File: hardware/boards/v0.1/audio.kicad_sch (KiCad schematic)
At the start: 30 parts, among them J10 MIDI_IN, J11 MIDI_OUT, J4 SPKR_L, J5 SPKR_R, J8 LINE_OUT, J9 LINE_IN, U24 MIC, U28 TS5A23159RSE, U29 NAU88C22YG

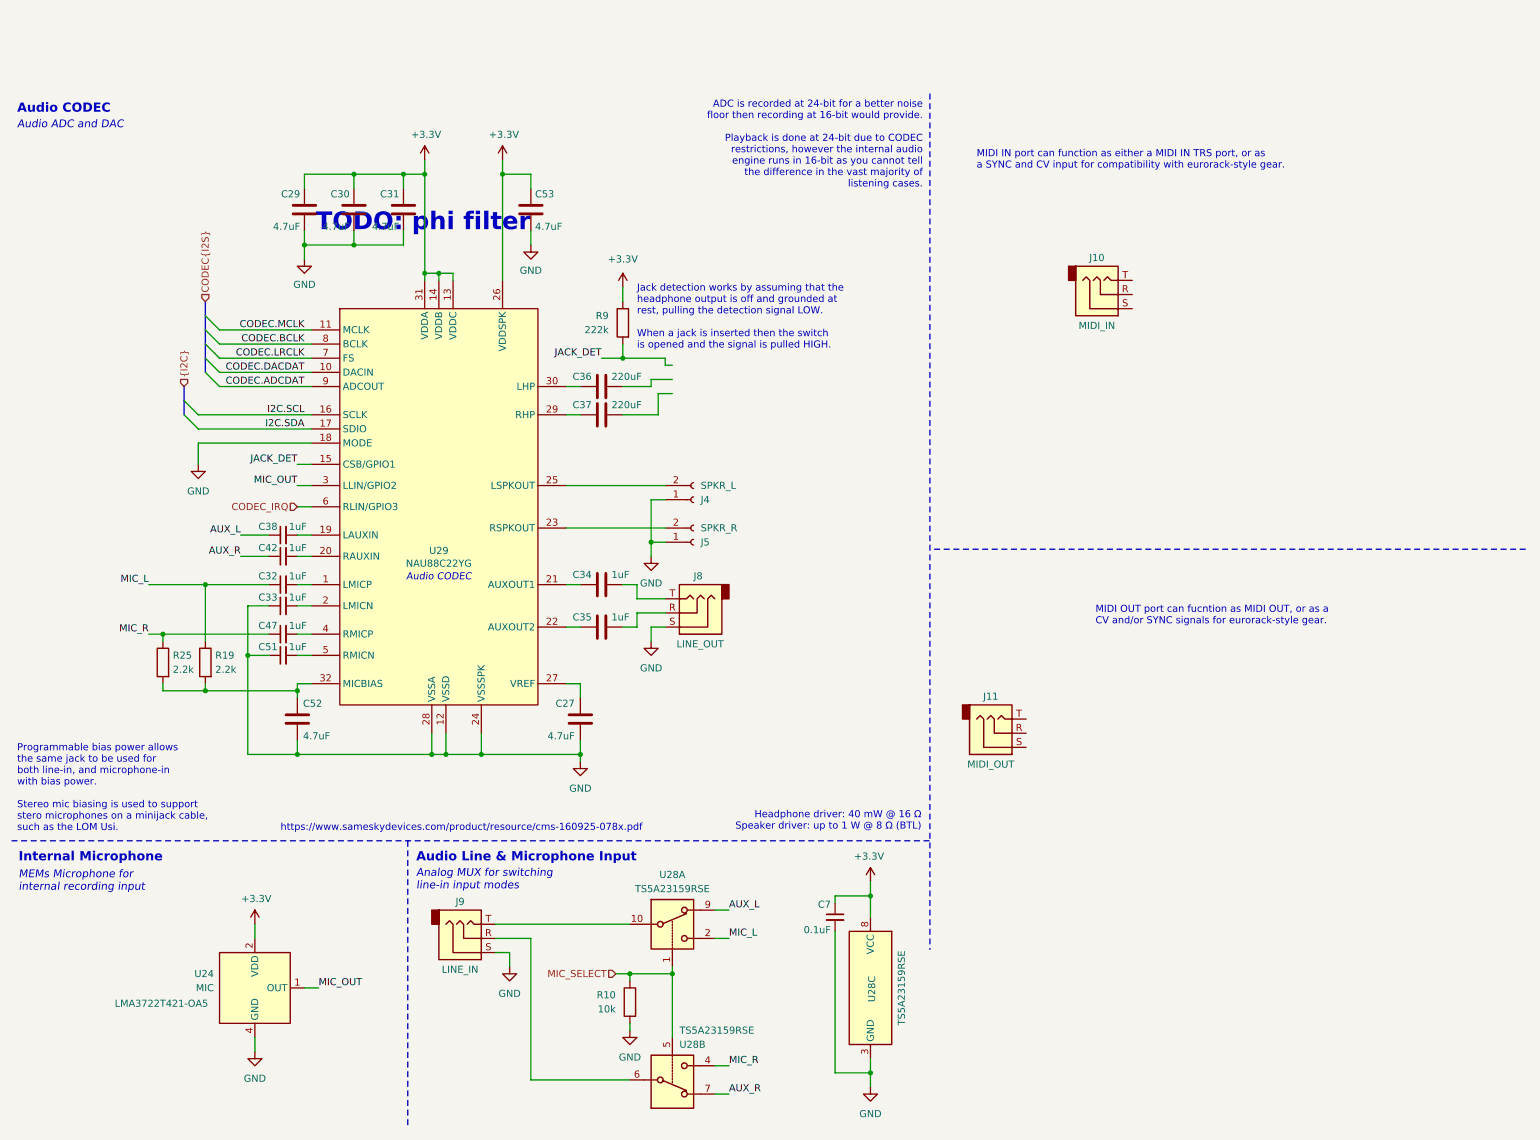
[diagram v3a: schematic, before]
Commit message: feat: start MIDI and CV schematic
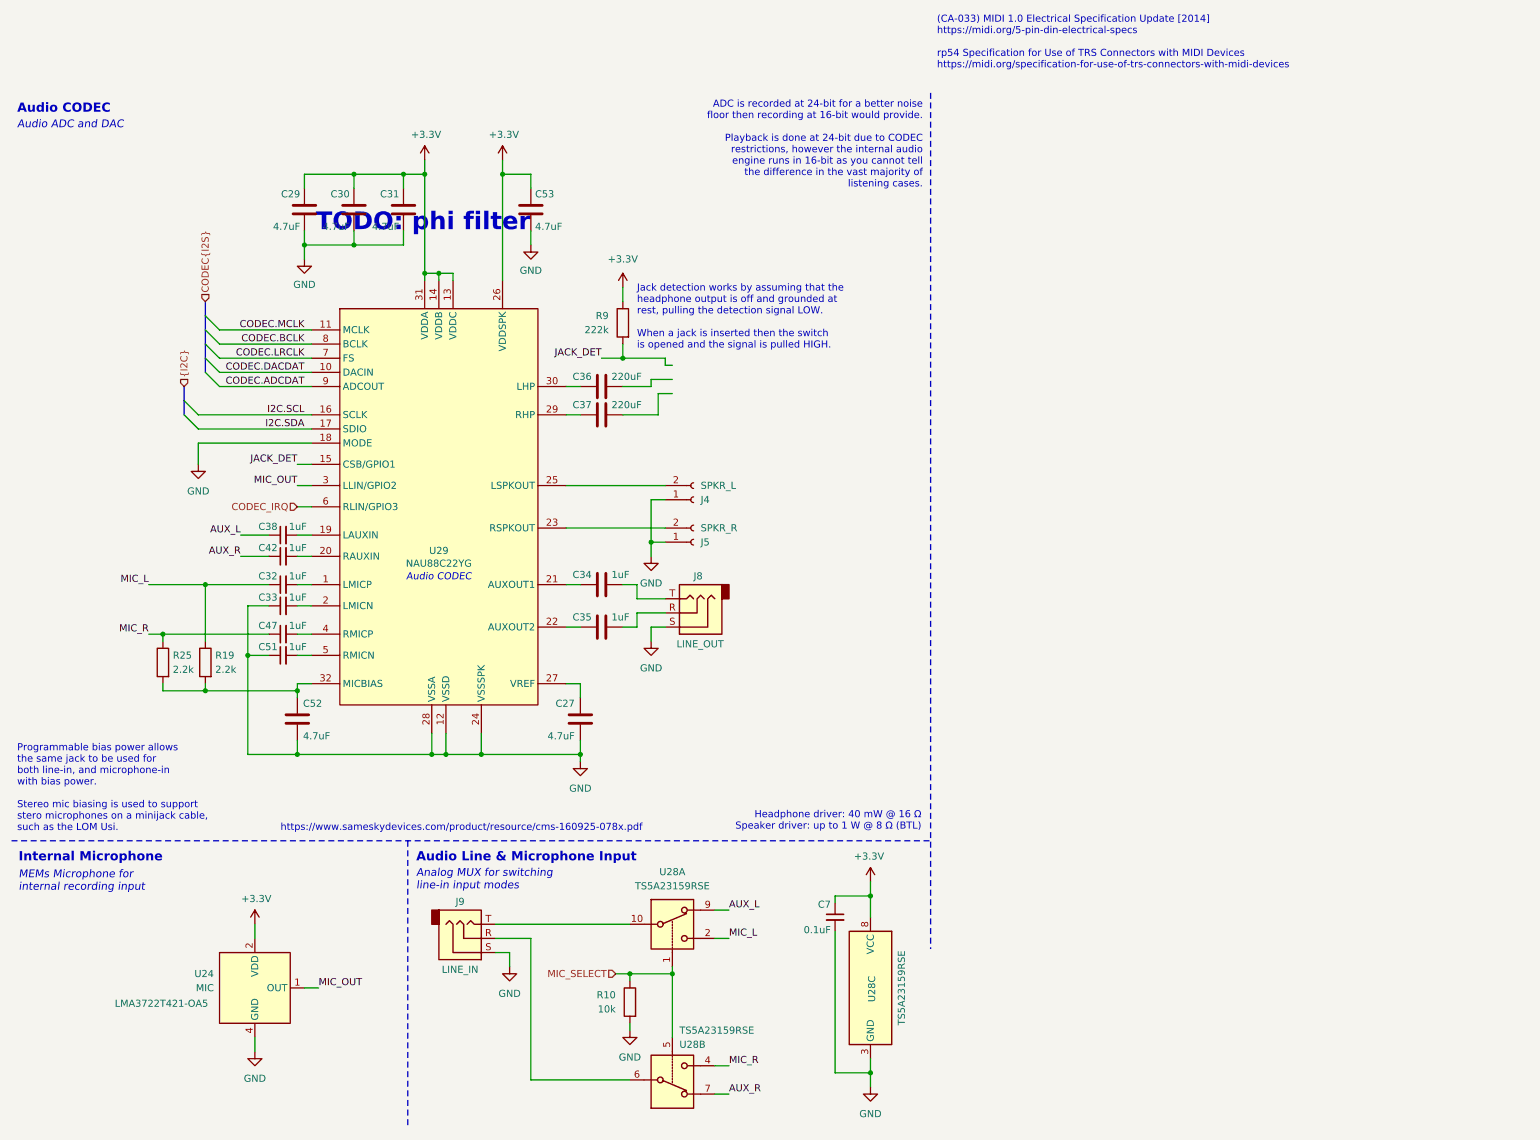
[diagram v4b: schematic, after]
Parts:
- removed J10: MIDI_IN, rhais_connector-lumberg:1503-02, symbol Connector_Audio:AudioJack3
- removed J11: MIDI_OUT, rhais_connector-lumberg:1503-02, symbol Connector_Audio:AudioJack3
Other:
- note added: "(CA-033) MIDI 1.0 Electrical Specification Update [2014] https://midi.org/5-pin-din-electrical-specs rp54 Specification for Use of TRS Connectors with MIDI Devices https://midi.org/specification-for-use-of-trs-connectors-with-midi-devices"
- note removed: "MIDI IN port can function as either a MIDI IN TRS port, or as a SYNC and CV input for compatibility with eurorack-style gear."
- note removed: "MIDI OUT port can fucntion as MIDI OUT, or as a CV and/or SYNC signals for eurorack-style gear."

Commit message: feat: various schematic organization
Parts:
- added TP20: LHP, TestPoint:TestPoint_Pad_D2.5mm, symbol Connector:TestPoint
- added TP21: RHP, TestPoint:TestPoint_Pad_D2.5mm, symbol Connector:TestPoint
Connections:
- net at C37.2: now also TP21.1
- net at C36.2: now also TP20.1
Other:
- moved on the sheet: C27, C29, C30, C31, C32, C33, C34, C35, C36, C37, C38, C42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

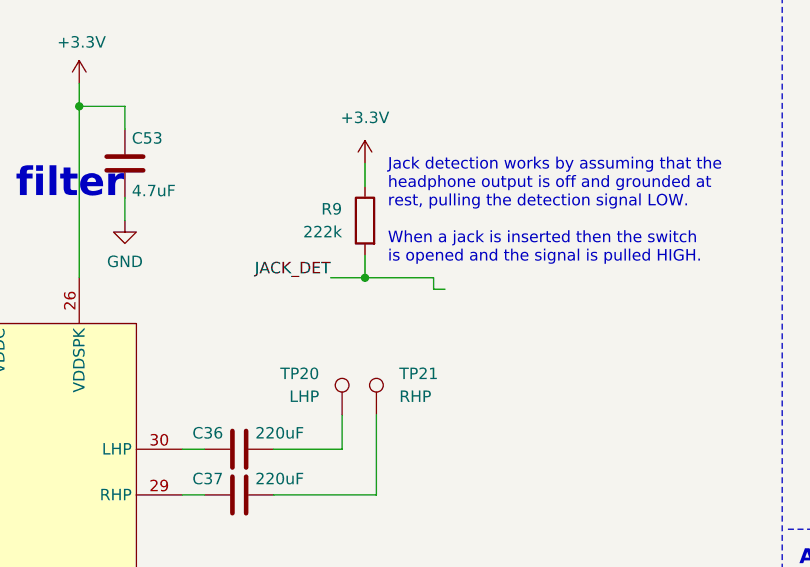
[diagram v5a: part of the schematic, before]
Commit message: feat: schematic organization, MIDI port routing
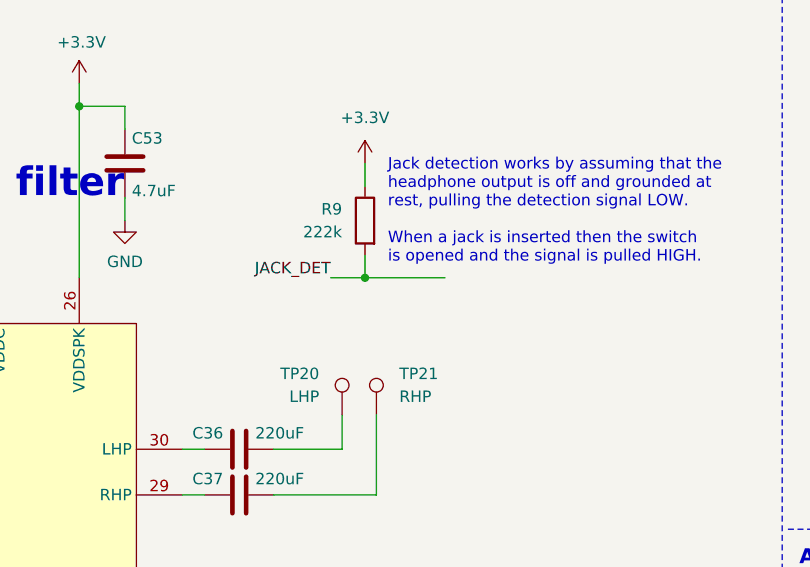
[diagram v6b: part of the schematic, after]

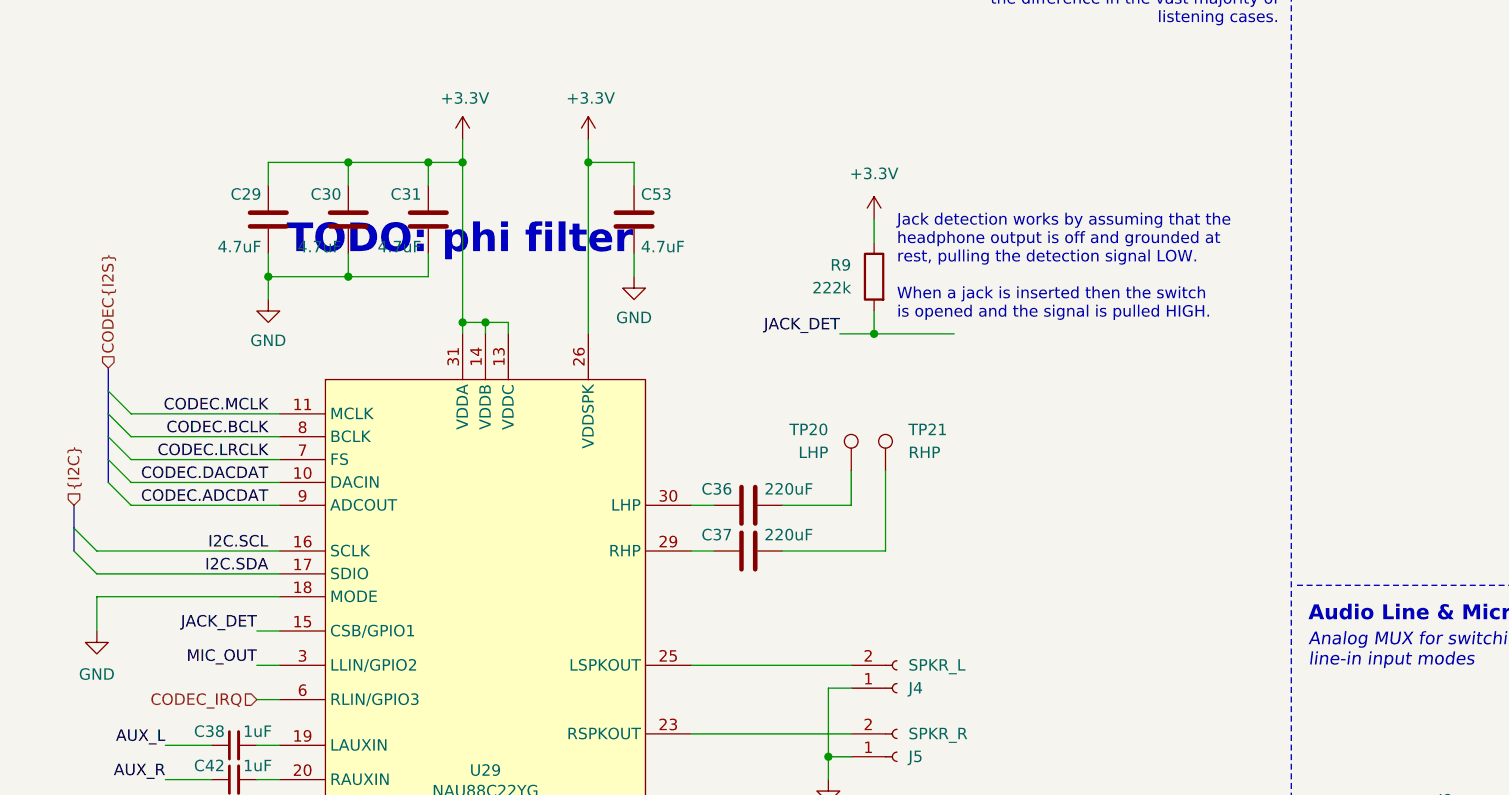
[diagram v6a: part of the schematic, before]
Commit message: feat: route audio components
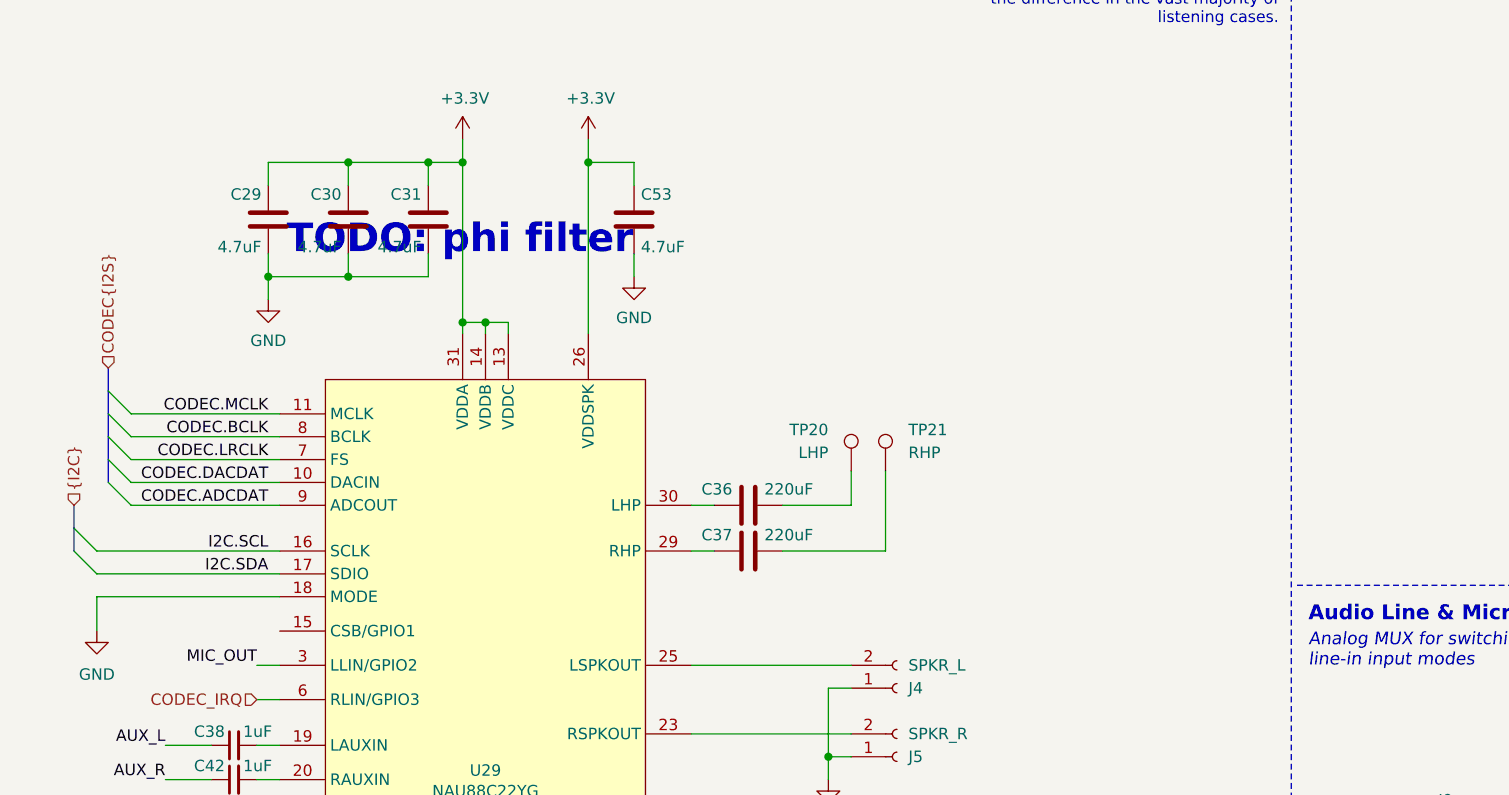
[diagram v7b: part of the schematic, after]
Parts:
- removed R9: 222k, Resistor_SMD:R_0201_0603Metric, symbol Device:R
- C27, C29, C30, C31, C32, C33, C34, C35, C38, C42, C47, C51, C52, C53, C7: footprint Capacitor_SMD:C_0201_0603Metric -> Capacitor_SMD:C_0603_1608Metric
- C36, C37: footprint Capacitor_SMD:C_0201_0603Metric -> Capacitor_SMD:C_0402_1005Metric
- R10, R19, R25: footprint Resistor_SMD:R_0201_0603Metric -> Resistor_SMD:R_0603_1608Metric
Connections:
- net JACK_DET: no longer names the net of U29.15 (CSB/GPIO1)
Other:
- note removed: "Jack detection works by assuming that the headphone output is off and grounded at rest, pulling the detection signal LOW. When a jack is inserted then the switch is opened and the signal is pulled HIGH."
